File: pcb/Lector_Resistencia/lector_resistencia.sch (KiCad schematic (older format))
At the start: 6 parts, among them J1 RJ45, J2 JACK_5P

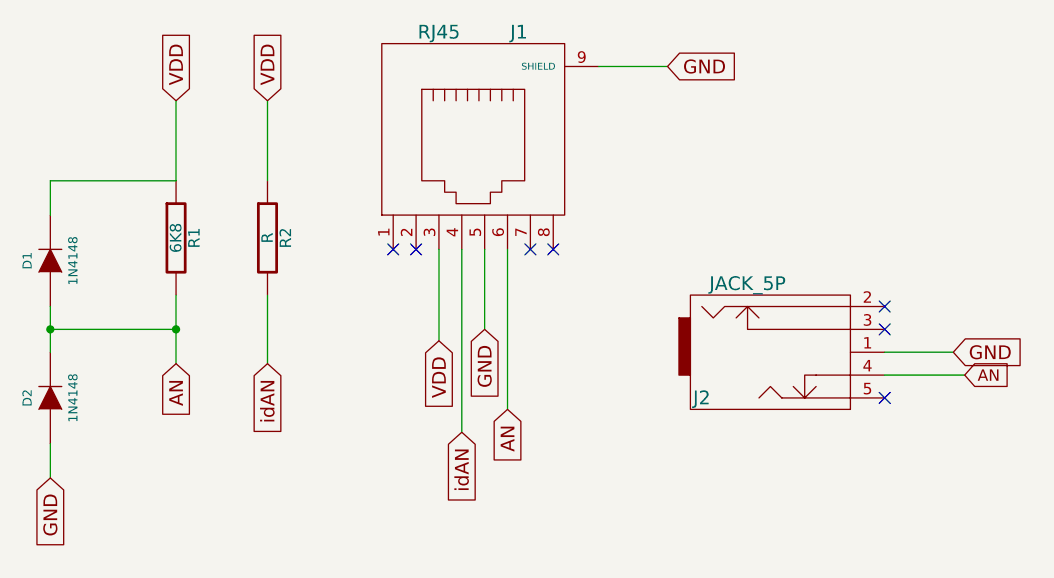
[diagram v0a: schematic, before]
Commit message: added 22k resistence
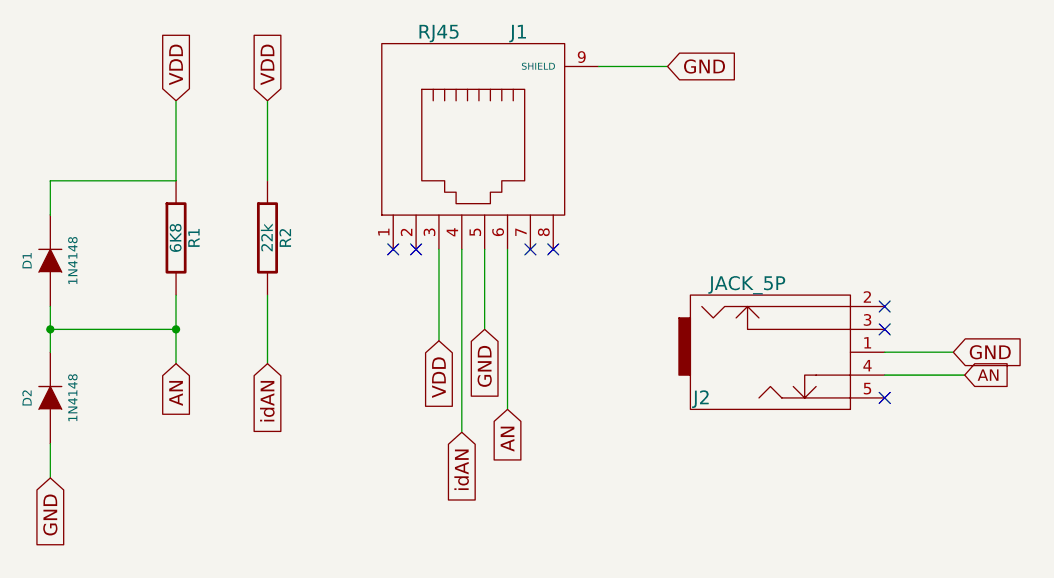
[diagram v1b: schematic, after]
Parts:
- R2: value R -> 22k
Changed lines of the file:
@@
-EESchema Schematic File Version 2  date mar 06 nov 2012 20:37:46 UYST
+EESchema Schematic File Version 2  date mié 07 nov 2012 19:44:20 UYST
 LIBS:power
 LIBS:device
@@
 LIBS:contrib
 LIBS:valves
+LIBS:lector_resistencia-cache
 EELAYER 25  0
 EELAYER END
@@
 Sheet 1 1
 Title "Módulo medidor de resistencia "
-Date "6 nov 2012"
+Date "7 nov 2012"
 Rev "1.1"
 Comp "Butiá"
@@
 P 4300 3950
 F 0 "R2" V 4380 3950 50  0000 C CNN
-F 1 "R" V 4300 3950 50  0000 C CNN
+F 1 "22k" V 4300 3950 50  0000 C CNN
 	1    4300 3950
 	1    0    0    -1
